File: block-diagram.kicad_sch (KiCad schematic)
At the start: 0 parts

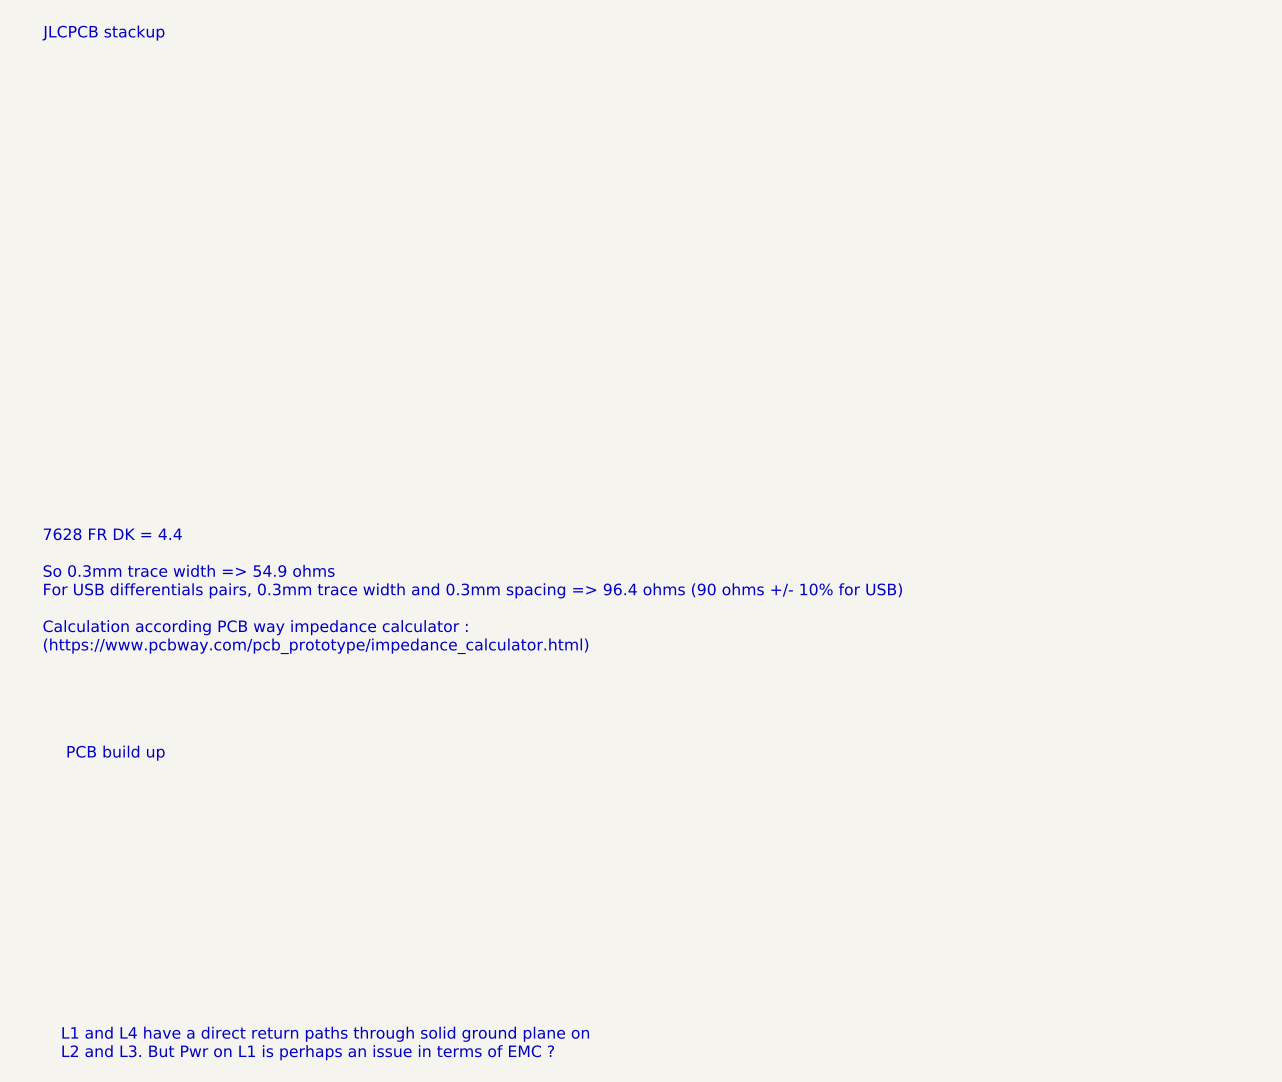
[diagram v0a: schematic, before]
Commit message: Set trace width and spacing for diff pairs from 0.3mm to 0.35mm for more precision on characteristic impedance
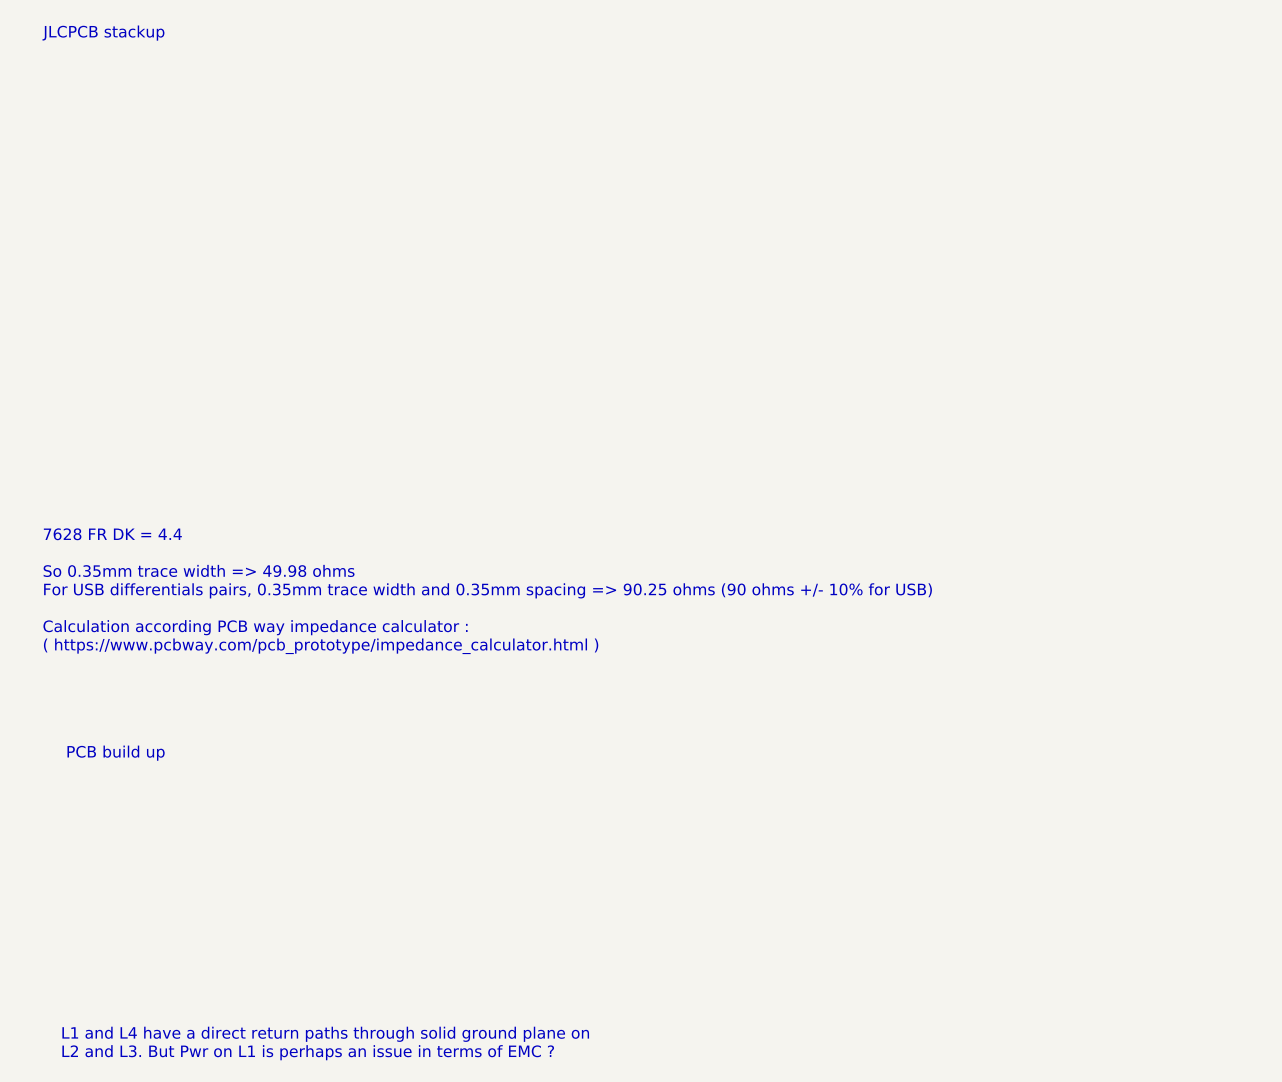
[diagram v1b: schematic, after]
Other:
- note added: "7628 FR DK = 4.4 So 0.35mm trace width => 49.98 ohms For USB differentials pairs, 0.35mm trace width and 0.35mm spacing => 90.25 ohms (90 ohms +/- 10% for USB) Calculation according PCB way impedance calculator : ( https://www.pcbway.com/pcb_prototype/impedance_calculator.html )"
- note removed: "7628 FR DK = 4.4 So 0.3mm trace width => 54.9 ohms For USB differentials pairs, 0.3mm trace width and 0.3mm spacing => 96.4 ohms (90 ohms +/- 10% for USB) Calculation according PCB way impedance calculator : (https://www.pcbway.com/pcb_prototype/impedance_calculator.html)"
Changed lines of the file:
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@@
 		)
 	)
-	(text "7628 FR DK = 4.4\n\nSo 0.3mm trace width => 54.9 ohms\nFor USB differentials pairs, 0.3mm trace width and 0.3mm spacing => 96.4 ohms (90 ohms +/- 10% for USB)\n\nCalculation according PCB way impedance calculator :\n(https://www.pcbway.com/pcb_prototype/impedance_calculator.html)"
+	(text "7628 FR DK = 4.4\n\nSo 0.35mm trace width => 49.98 ohms\nFor USB differentials pairs, 0.35mm trace width and 0.35mm spacing => 90.25 ohms (90 ohms +/- 10% for USB)\n\nCalculation according PCB way impedance calculator :\n( https://www.pcbway.com/pcb_prototype/impedance_calculator.html )"
 		(exclude_from_sim no)
 		(at 18.542 79.756 0)

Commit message: Modify the stackup to ease routing with ticker traces
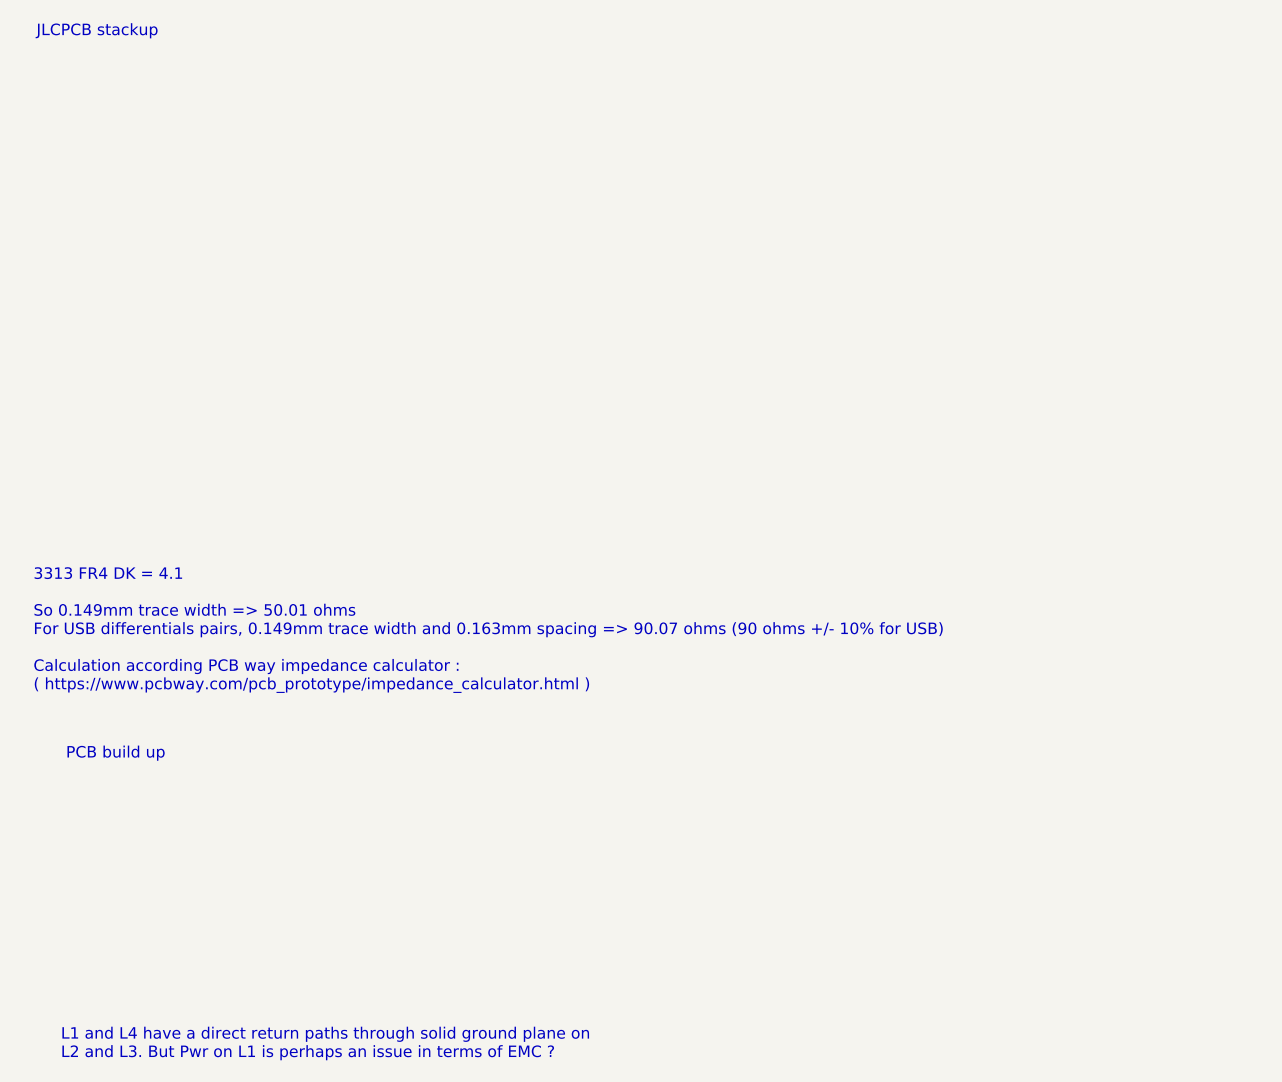
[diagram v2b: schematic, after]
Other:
- note added: "3313 FR4 DK = 4.1 So 0.149mm trace width => 50.01 ohms For USB differentials pairs, 0.149mm trace width and 0.163mm spacing => 90.07 ohms (90 ohms +/- 10% for USB) Calculation according PCB way impedance calculator : ( https://www.pcbway.com/pcb_prototype/impedance_calculator.html )"
- note removed: "7628 FR DK = 4.4 So 0.35mm trace width => 49.98 ohms For USB differentials pairs, 0.35mm trace width and 0.35mm spacing => 90.25 ohms (90 ohms +/- 10% for USB) Calculation according PCB way impedance calculator : ( https://www.pcbway.com/pcb_prototype/impedance_calculator.html )"
